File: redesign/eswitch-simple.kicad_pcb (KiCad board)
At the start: 4 copper layers, 136 x 104 mm, 210 parts, among them J11 CH1 OUTPUT, J12 CH2 OUTPUT, J13 CH3 OUTPUT, J14 CH4 OUTPUT, J15 CH5 OUTPUT, J16 CH6 OUTPUT, J17 CH7 OUTPUT, J18 CH8 OUTPUT, J2 BATT_RAW, J3 GND, J4 USB-C, J5 UART, Q5 BSC016N06NS, SW1 RESET, SW2 BOOT, U1 BTS7004-1EPP, U10 ESP32-S3-WROOM-1-N8, U11 SRV05-4HTG-D, U13 LM74800-Q1, U14 TLA431AIDBZR, U2 BTS7004-1EPP, U3 BTS7008-1EPR, U4 BTS7008-1EPR, U5 BTS7008-1EPR, U6 BTS7008-1EPR, U7 BTS7008-1EPR, U8 BTS7002-1EPP, U9 TPSM63603V3

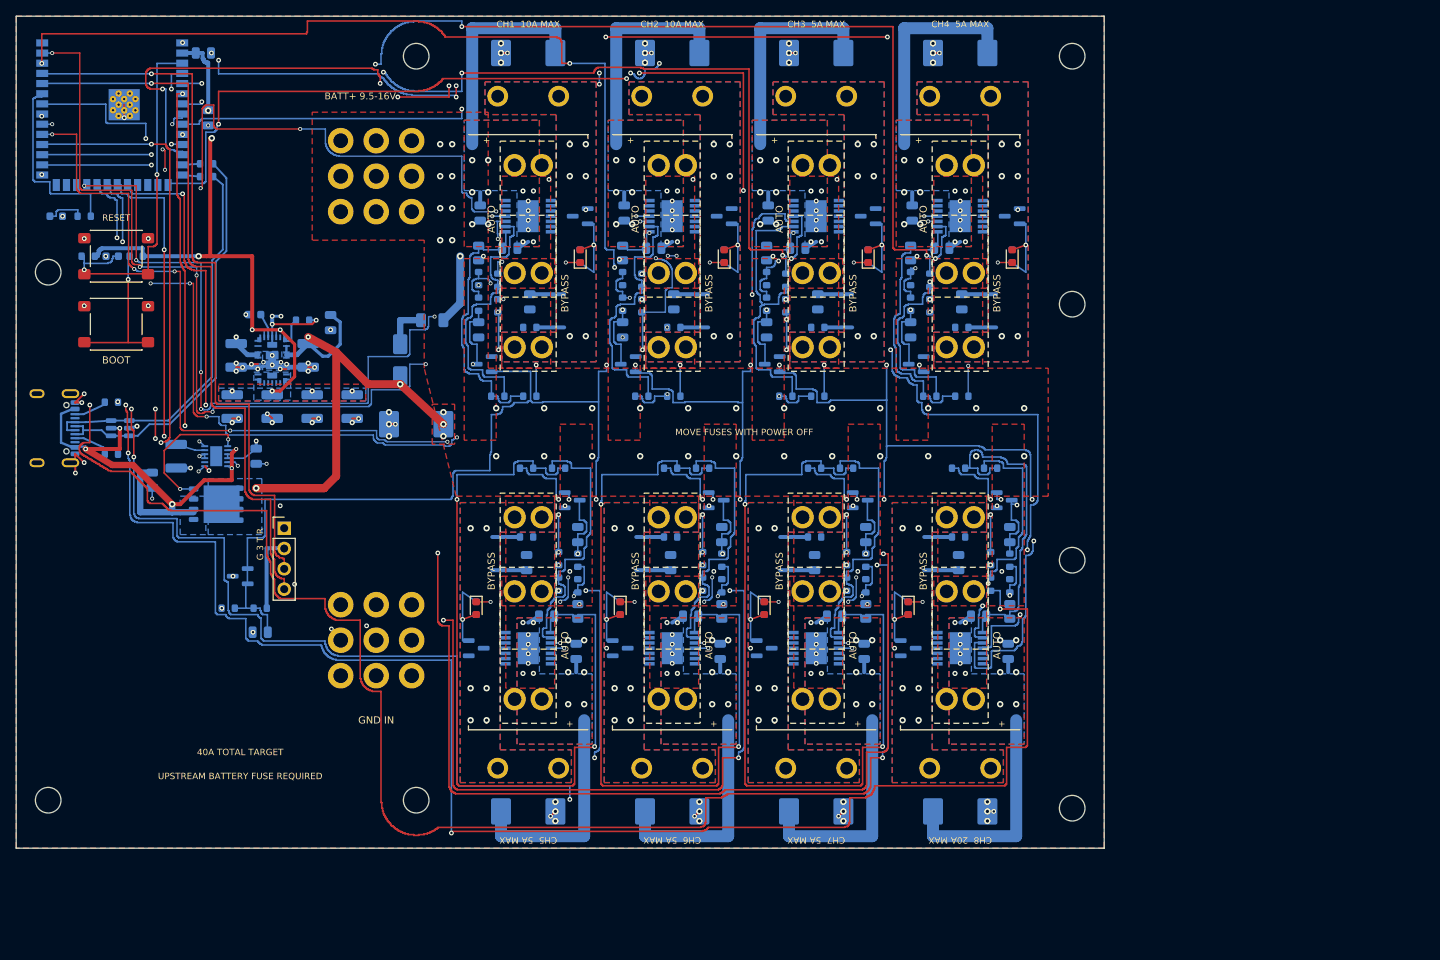
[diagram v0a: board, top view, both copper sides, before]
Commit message: Rework power copper and package expanded prototype for fabrication
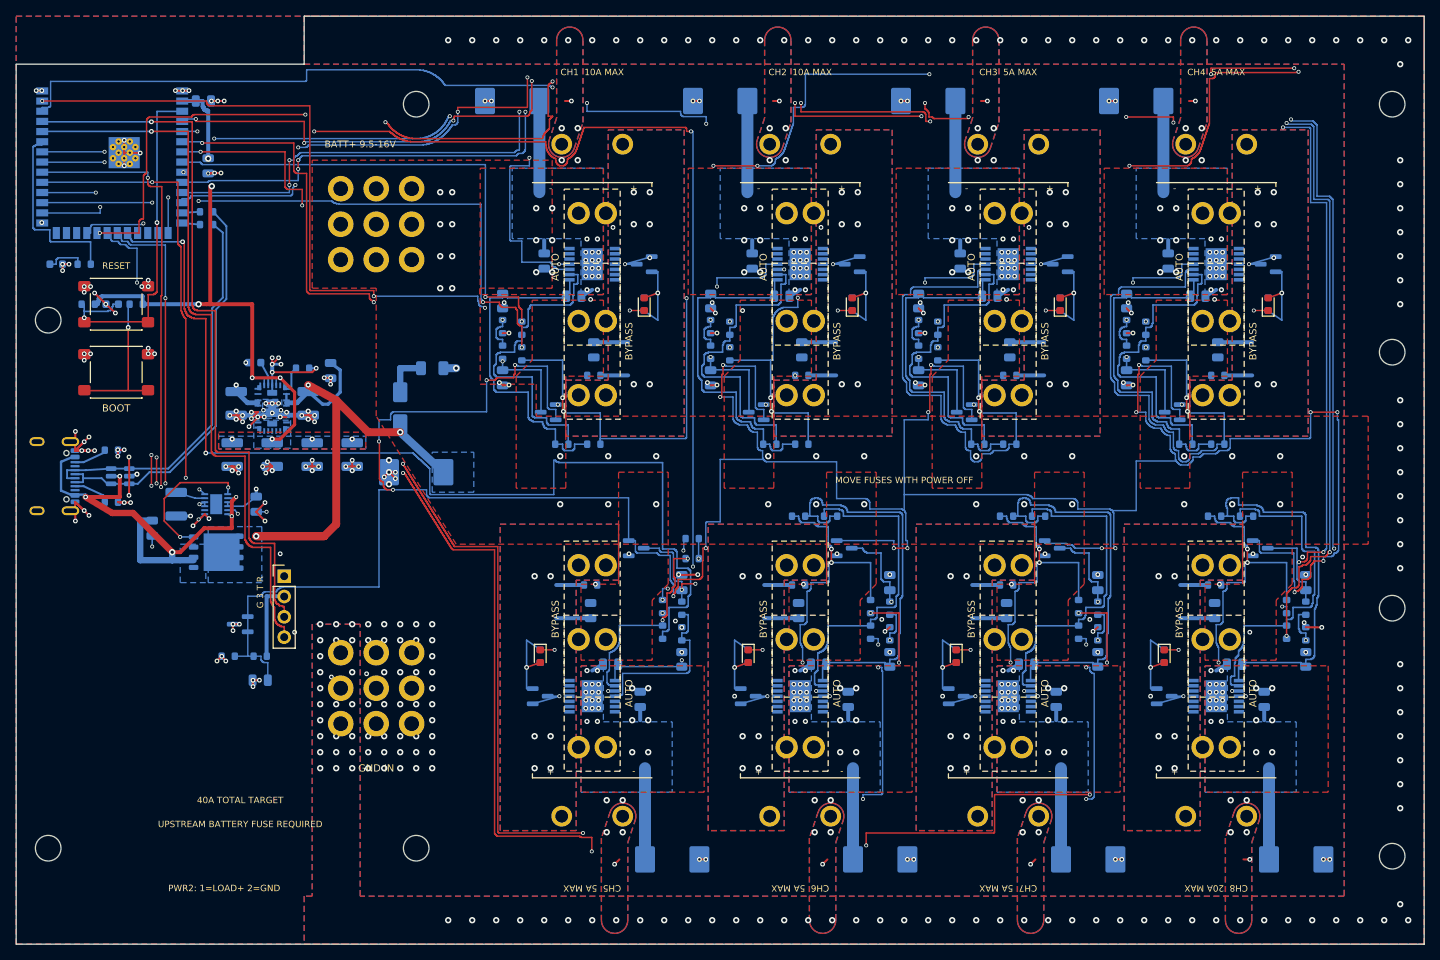
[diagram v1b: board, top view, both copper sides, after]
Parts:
- moved D804 42.4 mm to (160.0, 105.4)
- moved H5 40.4 mm to (172.0, 11.0)
- moved H6 40.4 mm to (172.0, 42.0)
- moved H7 40.4 mm to (172.0, 74.0)
- moved H8 40.4 mm to (172.0, 105.0)
- moved R801 37.5 mm to (158.8, 77.0)
- moved R802 37.5 mm to (158.8, 73.8)
- moved C803 37.5 mm to (161.2, 70.8)
- moved R803 37.5 mm to (161.2, 80.4)
- moved R804 37.5 mm to (161.2, 77.2)
- moved R805 37.5 mm to (161.2, 74.0)
- moved D704 34.5 mm to (134.0, 105.4)
- moved C802 32.6 mm to (149.8, 74.3)
- moved C804 32.6 mm to (152.3, 81.0)
- moved R806 32.6 mm to (149.8, 71.1)
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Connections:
- J11 pad 1: /GND -> /LOAD1
- J11 pad 2: /LOAD1 -> /GND
- J12 pad 1: /GND -> /LOAD2
- J12 pad 2: /LOAD2 -> /GND
- J13 pad 1: /GND -> /LOAD3
- J13 pad 2: /LOAD3 -> /GND
- J14 pad 1: /GND -> /LOAD4
- J14 pad 2: /LOAD4 -> /GND
- J15 pad 1: /GND -> /LOAD5
- J15 pad 2: /LOAD5 -> /GND
- J16 pad 1: /GND -> /LOAD6
- J16 pad 2: /LOAD6 -> /GND
- J17 pad 1: /GND -> /LOAD7
- J17 pad 2: /LOAD7 -> /GND
- J18 pad 1: /GND -> /LOAD8
- J18 pad 2: /LOAD8 -> /GND
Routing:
- net /ADC_CLAMP_2V5: track 234.3 -> 424.5 mm, vias 14 -> 20
- net /DEN2: track 118.3 -> 285.4 mm, vias 4 -> 7
- net /GND: track 61.1 -> 196.2 mm, vias 140 -> 440
- net /DENR1: track 28.1 -> 118.8 mm
- net /DEN6: track 139.9 -> 223.8 mm, vias 6 -> 4
- net /UGND5: track 104.1 -> 28.9 mm
- net /DEN5: track 118.4 -> 189.4 mm, vias 6 -> 3
- net /DEN4: track 303.5 -> 232.7 mm, vias 5 -> 4
- net /UGND6: track 104.1 -> 53.4 mm, vias 2 -> 0
- net /UGND7: track 104.0 -> 53.4 mm, vias 2 -> 0
- net /IS5: track 180.7 -> 144.3 mm, vias 2 -> 6
- net /DENR4: track 35.7 -> 71.2 mm, vias 3 -> 2
- net /DENR3: track 39.1 -> 71.2 mm, vias 4 -> 2
- net /IN5: track 164.8 -> 133.2 mm, vias 5 -> 2
- net /IS7: track 216.7 -> 246.4 mm, vias 4 -> 7
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- removed copper zone on F.Cu, net /VIN
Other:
- board size 136 x 104 mm -> 176 x 116 mm
- board text added: "PWR2: 1=LOAD+ 2=GND"
